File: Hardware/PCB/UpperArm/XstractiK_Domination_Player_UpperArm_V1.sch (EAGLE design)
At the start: 21 parts, among them Q1 MMBT2222, Q2 AO3401A, U1 ESP32-DEVKITC-32U, U2 RFM95W-915S2, U3 MCP73831T-3ACI/OT, U4 AP2112K-3.3TRG1

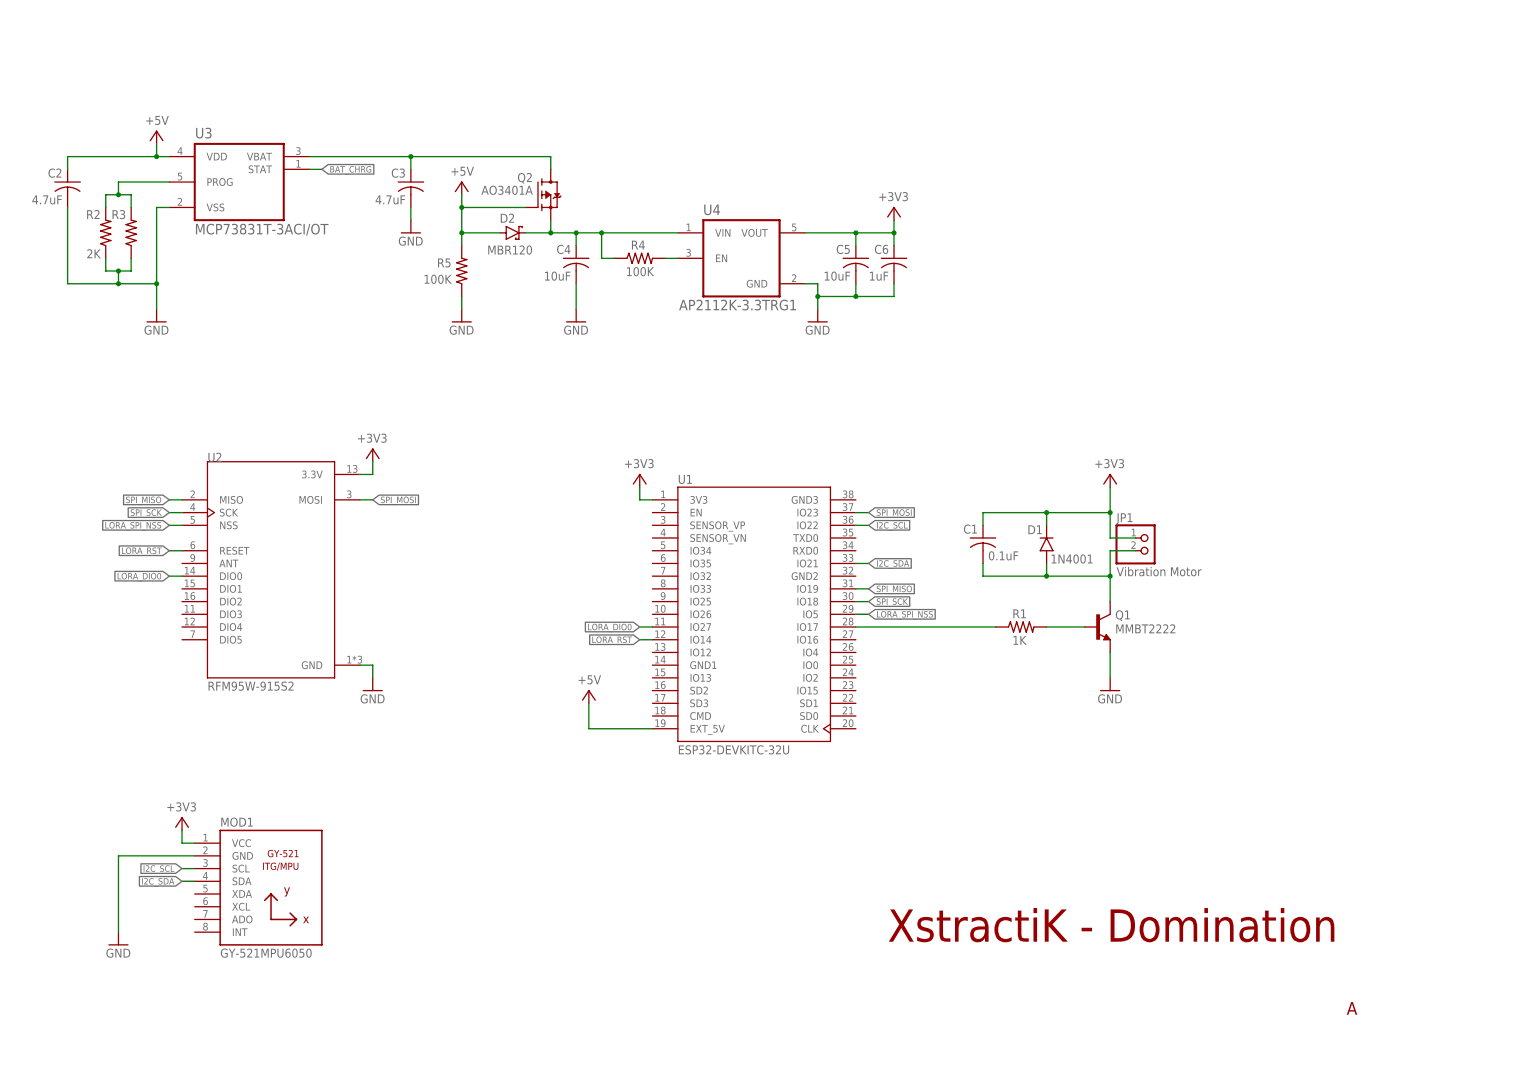
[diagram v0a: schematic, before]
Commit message: Schematic + Libraries + Datasheets
Schematic :
 - Li-Ion battery fuel gauge (MAX17048G)
 - USB to UART bridge (CH340C)
 - Connectors for USB-C, Breakout pins, Li-Ion battery
 - Mount holes

Libraries :
 - Supply
 - Switches
 - Fuel gauge
 - Li-Ion battery

Datasheets :
 - Li-Ion battery fuel gauge (MAX17048G)
 - USB to UART bridge (CH340C)
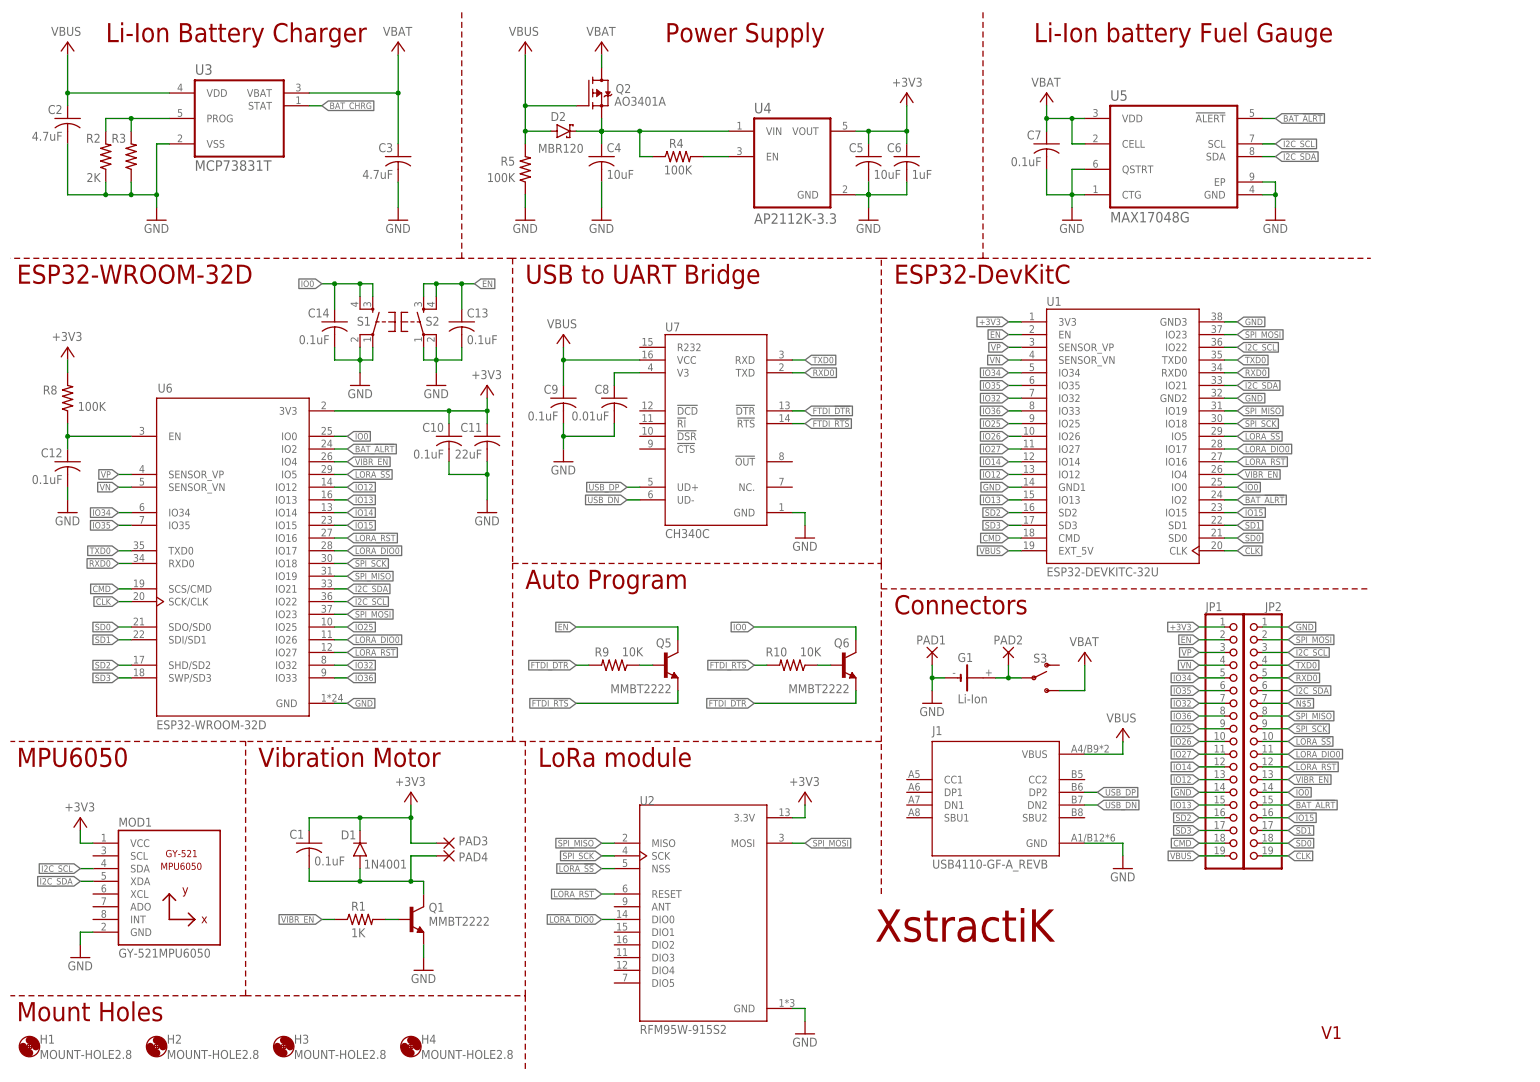
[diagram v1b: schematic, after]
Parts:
- added C10, C12, C13, C14, C7, C9: 0.1uF, rcl:C-USC0805
- added C11: 22uF, rcl:C-USC0805
- added C8: 0.01uF, rcl:C-USC0805
- added G1: Li-Ion, battery:CR-AA
- added H1, H2, H3, H4: MOUNT-HOLE2.8, holes:MOUNT-HOLE2.8
- added J1: USB4110-GF-A_REVB, USB-C-SMD:USB4110-GF-A_REVB
- added JP2: (no value), pinhead:PINHD-1X19
- added PAD1, PAD2, PAD3, PAD4: (no value), wirepad:SMD5
- added Q5, Q6: MMBT2222, MMBT2222:MMBT2222
- added R10, R9: 10K, rcl:R-US_R0805
- added R8: 100K, rcl:R-US_R0805
- added S1, S2: (no value), Switches:MOMENTARY-SWITCH-SPST-2-SMD-5.2MM
- added S3: (no value), Switches:SWITCH-SPDT-SMD-RIGHT-ANGLE
- added U5: MAX17048G, MAX17048G:MAX17048G
- added U6: ESP32-WROOM-32D, ESP32-WROOM-32D:ESP32-WROOM-32D
- added U7: CH340C, CH340C:CH340C
- JP1: value Vibration Motor -> (none); device pinhead:PINHD-1X2 -> pinhead:PINHD-1X19
- U3: value MCP73831T-3ACI/OT -> MCP73831T; device MCP73831T-3ACI_OT:MCP73831T-3ACI/OT -> MCP73831T-3ACI_OT:MCP73831T
- U4: value AP2112K-3.3TRG1 -> AP2112K-3.3; device AP2112K-3.3TRG1:AP2112K-3.3TRG1 -> AP2112K-3.3TRG1:AP2112K-3.3
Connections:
- removed net +5V: C2.1, D2.A, Q2.G, R5.2, U1.EXT_5V, U3.VDD
- removed net LORA_SPI_NSS: U1.IO5, U2.NSS
- new net BAT_!ALRT: JP2.15, U1.IO2, U5.!ALERT, U6.IO2
- new net CLK: JP2.19, U1.CLK, U6.SCK/CLK
- new net CMD: JP1.18, U1.CMD, U6.SCS/CMD
- new net EN: C12.1, C13.1, JP1.2, Q5.C, R8.1, S2.3, S2.4, U1.EN, U6.EN
- new net FTDI_!DTR: Q6.E, R9.2, U7.!DTR
- new net FTDI_!RTS: Q5.E, R10.2, U7.!RTS
- new net IO0: C14.1, JP2.14, Q6.C, S1.3, S1.4, U1.IO0, U6.IO0
- new net IO12: JP1.13, U1.IO12, U6.IO12
- new net IO13: JP1.15, U1.IO13, U6.IO13
- new net IO14: JP1.12, U1.IO14, U6.IO14
- new net IO15: JP2.16, U1.IO15, U6.IO15
- new net IO25: JP1.9, U1.IO25, U6.IO25
- new net IO26: JP1.10, U1.IO26
- new net IO27: JP1.11, U1.IO27
- new net IO32: JP1.7, U1.IO32, U6.IO32
- new net IO34: JP1.5, U1.IO34, U6.IO34
- new net IO35: JP1.6, U1.IO35, U6.IO35
- new net IO36: JP1.8, U1.IO33, U6.IO33
- new net LORA_!SS: JP2.10, U1.IO5, U2.NSS, U6.IO5
- new net N$5: JP2.7
- new net N$6: Q6.B, R10.1
- new net N$7: Q5.B, R9.1
- new net N$8: G1.+, PAD2.P, S3.P
- new net RXD0: JP2.5, U1.RXD0, U6.RXD0, U7.TXD
- new net SD0: JP2.18, U1.SD0, U6.SDO/SD0
- new net SD1: JP2.17, U1.SD1, U6.SDI/SD1
- new net SD2: JP1.16, U1.SD2, U6.SHD/SD2
- new net SD3: JP1.17, U1.SD3, U6.SWP/SD3
- new net TXD0: JP2.4, U1.TXD0, U6.TXD0, U7.RXD
- new net USB_DN: J1.DN2, U7.UD-
- new net USB_DP: J1.DP2, U7.UD+
- new net VBUS: C2.1, C9.1, D2.A, J1.VBUS, JP1.19, Q2.G, R5.2, U1.EXT_5V, U3.VDD, U7.VCC
- new net VIBR_EN: JP2.13, R1.1, U1.IO4, U6.IO4
- new net VN: JP1.4, U1.SENSOR_VN, U6.SENSOR_VN
- new net VP: JP1.3, U1.SENSOR_VP, U6.SENSOR_VP
- net +3V3: now also C10.1, C11.1, PAD3.P, R8.2, U6.3V3
- net GND: now also C10.2, C11.2, C12.2, C13.2, C14.2, C7.2, C8.2, C9.2, G1.-, J1.GND, JP1.14, JP2.1, PAD1.P, S1.1, S1.2, S2.1, S2.2, U1.GND1, U1.GND2, U1.GND3, U5.CTG, U5.EP, U5.GND, U5.QSTRT, U6.GND, U7.GND
- net I2C_SCL: now also JP2.3, MOD1.SDA, U5.SCL, U6.IO22; no longer MOD1.SCL
- net I2C_SDA: now also JP2.6, MOD1.XDA, U5.SDA, U6.IO21; no longer MOD1.SDA
- net LORA_DIO0: now also JP2.11, U1.IO17, U6.IO17, U6.IO26; no longer U1.IO27
- net LORA_RST: now also JP2.12, U1.IO16, U6.IO16, U6.IO27; no longer U1.IO14
- net N$1: now also PAD4.P; no longer JP1.2
- net N$3: now also C8.1, U7.V3; no longer R1.1, U1.IO17
- net SPI_MISO: now also JP2.8, U6.IO19
- net SPI_MOSI: now also JP2.2, U6.IO23
- net SPI_SCK: now also JP2.9, U6.IO18
- net VBAT: now also C7.1, S3.S, U5.CELL, U5.VDD
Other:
- note added: "Auto Program"
- note added: "Connectors"
- note added: "ESP32-DevKitC"
- note added: "ESP32-WROOM-32D"
- note added: "Li-Ion Battery Charger"
- note added: "Li-Ion battery Fuel Gauge"
- note added: "LoRa module"
- note added: "MPU6050"
- note added: "Mount Holes"
- note added: "Power Supply"
- note added: "USB to UART Bridge"
- note added: "V1"
- note added: "Vibration Motor"
- note added: "XstractiK"
- note removed: "A"
- note removed: "XstractiK - Domination"
- moved on the sheet: C1, C2, C3, C4, C5, C6, D1, D2, MOD1, Q1, Q2, R1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

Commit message: Add RTC Clock 32.768 kHz
DS3231 used as external RTC clock for ESP32
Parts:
- added C15: 100nF, rcl:C-USC0805
- added R11: 100K, rcl:R-US_R0805
- added R6: 680K, rcl:R-US_R0805
- added R7: 220K, rcl:R-US_R0805
- added U8: DS3231SN, DS3231SN:DS3231SN
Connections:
- removed net IO32: JP1.7, U1.IO32, U6.IO32
- removed net IO36: JP1.8, U1.IO33, U6.IO33
- removed net N$5: JP2.7
- new net 32K_XN: C13.1, JP1.8, U1.IO33, U6.IO33
- new net 32K_XP: JP1.7, R11.1, U1.IO32, U6.IO32, U8.32KHZ
- net +3V3: now also C15.1, R6.2, U8.VCC
- net BAT_CHRG: now also U1.IO15, U6.IO15
- net EN: no longer C13.1
- net GND: now also C15.2, JP2.7, R7.1, U8.GND, U8.VBAT
- net IO15: no longer U1.IO15, U6.IO15
- net IO26: now also U6.IO26
- net IO27: now also U6.IO27
- net LORA_DIO0: no longer U6.IO26
- net LORA_RST: no longer U6.IO27
- net VBUS: now also R11.2, R6.1, R7.2
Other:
- note added: "BackUp Switches"
- note added: "DTR RTS --> EN IO0 1 1 1 1 0 0 1 1 1 0 0 1 0 1 1 0"
- note added: "RTC Clock"

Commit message: Schematic + Library + Datasheet
Add 3-axis Magnetic sensor module (HMC5883)
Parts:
- removed C13: 0.1uF, rcl:C-USC0805
- added C16: 0.1uF, rcl:C-USC0805
- added U9: QMC5883GY-271, QMC5883:QMC5883GY-271
- G1: value Li-Ion -> Lithium
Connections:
- net LORA_RST renamed LORA_!RST
- new net VCC: U9.VCC
- net 32K_XN: now also C16.1; no longer C13.1, U6.IO33
- net GND: now also C16.2, U9.GND; no longer C13.2
- net I2C_SCL: now also U9.SCL
- net I2C_SDA: now also U9.SDA
- net SPI_MISO: now also JP2.2, U1.IO23
- net SPI_MOSI: no longer JP2.2, U1.IO23
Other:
- note added: "9-Axis IMU"
- note added: "Lithium Battery Charger"
- note added: "Lithium battery Fuel Gauge"
- note added: "XstractiK - Domination"
- note removed: "Li-Ion Battery Charger"
- note removed: "Li-Ion battery Fuel Gauge"
- note removed: "MPU6050"
- note removed: "XstractiK"
- moved on the sheet: C1, C15, D1, H1, H2, H3, H4, MOD1, PAD3, PAD4, Q1, Q5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
